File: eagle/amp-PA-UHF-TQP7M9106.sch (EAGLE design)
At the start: 27 parts, among them Q3 MOSFET-P-N-PAIR, U1 TQP7M9106, X1 SMA-142-0701-801/806, X2 SMA-142-0701-801/806

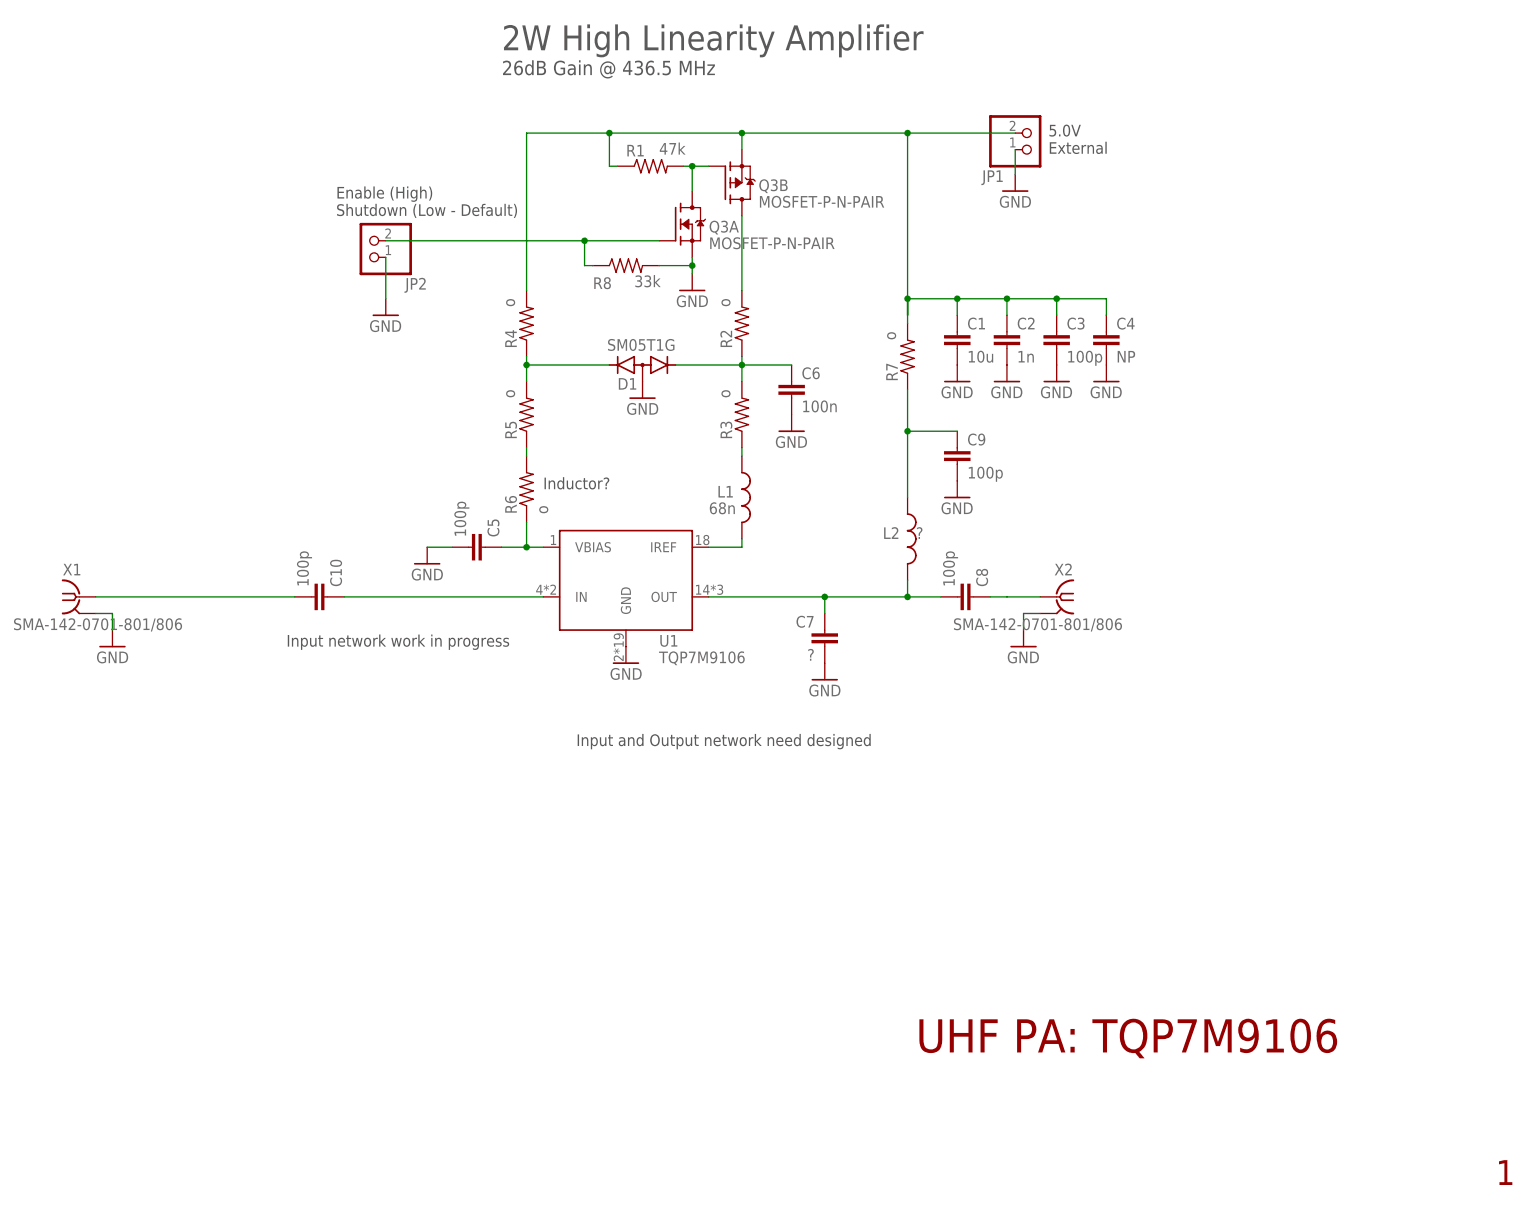
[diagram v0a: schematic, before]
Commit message: PA TQP7M9206, some updates, desgin will most likely use TQP7M9205
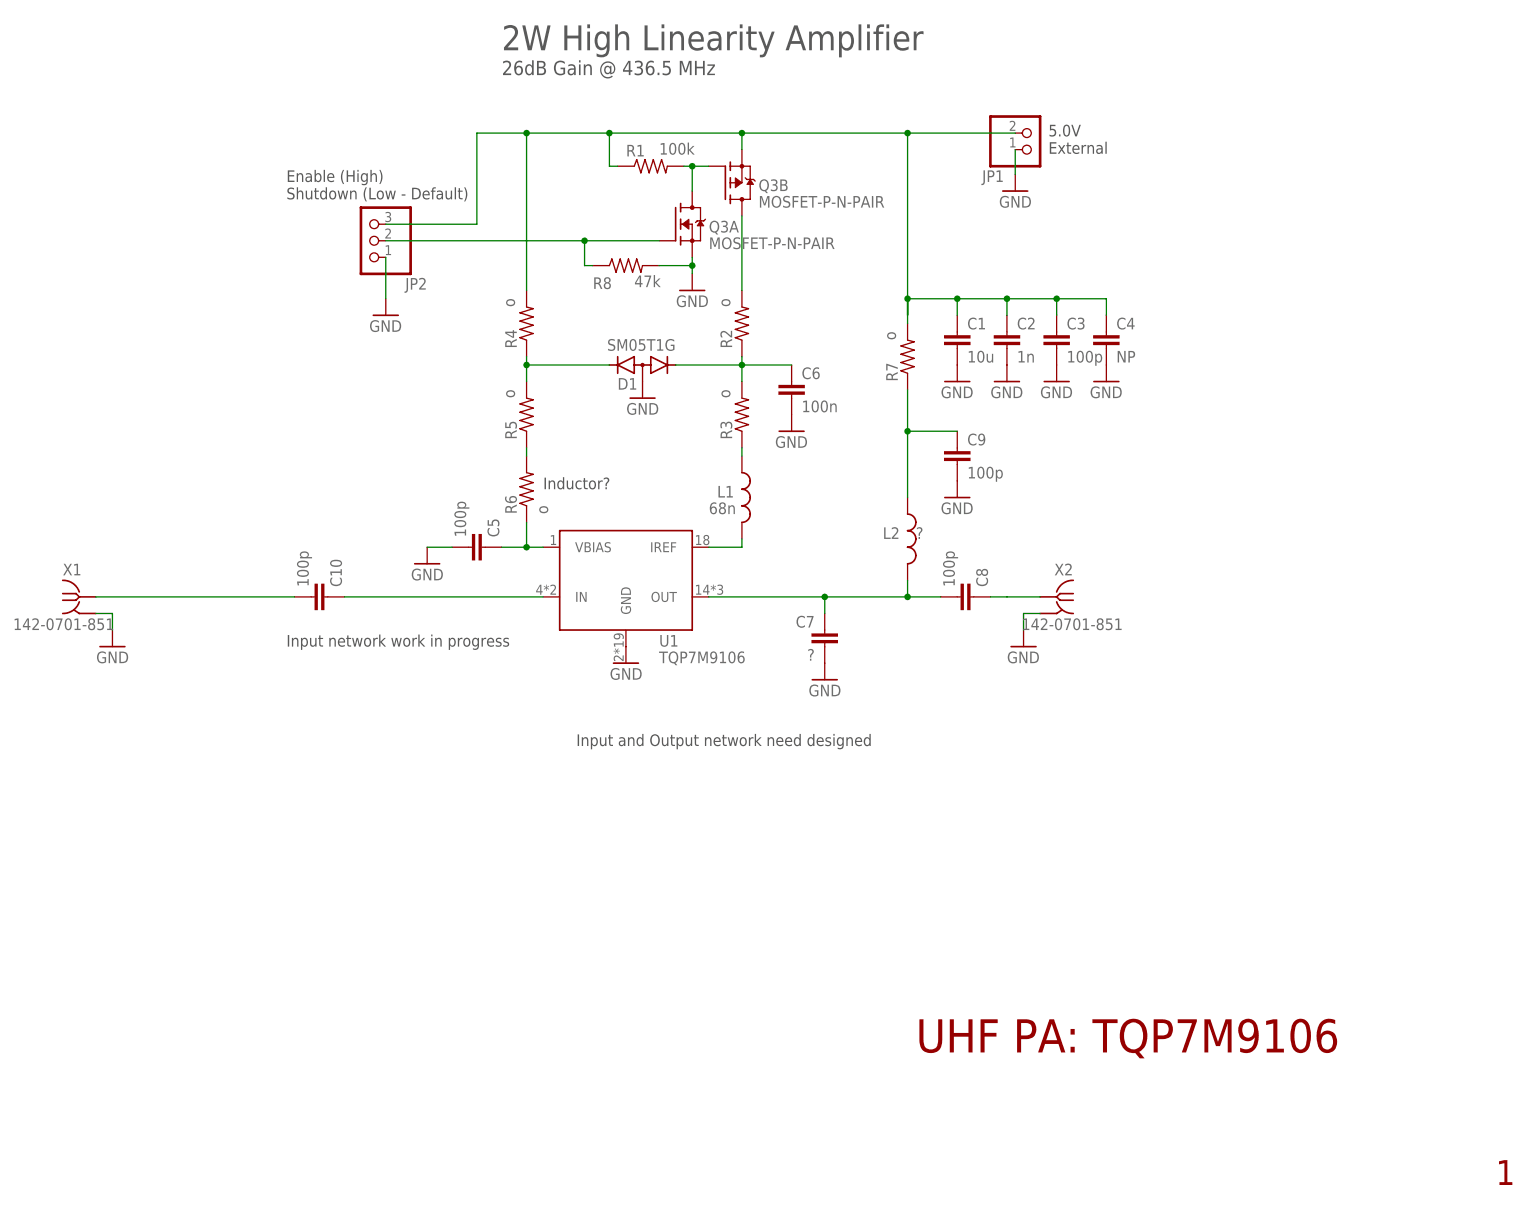
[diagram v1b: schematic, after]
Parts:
- JP2: device pinhead:PINHD-1X2 -> pinhead:PINHD-1X3
- R1: value 47k -> 100k
- R8: value 33k -> 47k
- X1, X2: value SMA-142-0701-801/806 -> 142-0701-851; device con-coax:SMA-142-0701-801/806 -> J-Cinch-142-0701-851-SMA-end-launch:142-0701-851
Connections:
- net GND: now also X1.GND, X2.GND; no longer X1.2, X2.2
- net N$6: now also X1.RF; no longer X1.1
- net N$67: now also X2.RF; no longer X2.1
- net N$72: now also JP2.3
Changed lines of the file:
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@@
 <part name="JP1" library="pinhead" library_urn="urn:adsk.eagle:library:325" deviceset="PINHD-1X2" device="" package3d_urn="urn:adsk.eagle:package:22435/2"/>
 <part name="GND70" library="supply1" library_urn="urn:adsk.eagle:library:371" deviceset="GND" device=""/>
-<part name="X1" library="con-coax" library_urn="urn:adsk.eagle:library:133" deviceset="SMA-" device="142-0701-801/806" package3d_urn="urn:adsk.eagle:package:6214/1"/>
+<part name="X1" library="J-Cinch-142-0701-851-SMA-end-launch" deviceset="142-0701-851" device=""/>
 <part name="GND71" library="supply1" library_urn="urn:adsk.eagle:library:371" deviceset="GND" device=""/>
 <part name="C8" library="oresat-rcl" deviceset="C-EU" device="0402-B-NOSILK" value="100p"/>
-<part name="X2" library="con-coax" library_urn="urn:adsk.eagle:library:133" deviceset="SMA-" device="142-0701-801/806" package3d_urn="urn:adsk.eagle:package:6214/1"/>
+<part name="X2" library="J-Cinch-142-0701-851-SMA-end-launch" deviceset="142-0701-851" device=""/>
 <part name="GND72" library="supply1" library_urn="urn:adsk.eagle:library:371" deviceset="GND" device=""/>
 <part name="L1" library="oresat-rcl" deviceset="L-US" device="0603-B-NOSILK" value="68n"/>
@@
 <part name="C3" library="oresat-rcl" deviceset="C-EU" device="0603-B-NOSILK" value="100p"/>
 <part name="GND103" library="supply1" library_urn="urn:adsk.eagle:library:371" deviceset="GND" device=""/>
-<part name="JP2" library="pinhead" library_urn="urn:adsk.eagle:library:325" deviceset="PINHD-1X2" device="" package3d_urn="urn:adsk.eagle:package:22435/2"/>
+<part name="JP2" library="pinhead" library_urn="urn:adsk.eagle:library:325" deviceset="PINHD-1X3" device="" package3d_urn="urn:adsk.eagle:package:22458/2"/>
 <part name="GND114" library="supply1" library_urn="urn:adsk.eagle:library:371" deviceset="GND" device=""/>
-<part name="R1" library="oresat-rcl" deviceset="R-US_" device="0402-B-NOSILK" value="47k"/>
+<part name="R1" library="oresat-rcl" deviceset="R-US_" device="0402-B-NOSILK" value="100k"/>
 <part name="R4" library="oresat-rcl" deviceset="R-US_" device="0805-B-NOSILK" value="o"/>
 <part name="R2" library="oresat-rcl" deviceset="R-US_" device="0805-B-NOSILK" value="o"/>
@@
 <part name="GND1" library="supply1" library_urn="urn:adsk.eagle:library:371" deviceset="GND" device=""/>
 <part name="C9" library="oresat-rcl" deviceset="C-EU" device="0603-B-NOSILK" value="100p"/>
-<part name="R8" library="oresat-rcl" deviceset="R-US_" device="0402-B-NOSILK" value="33k"/>
+<part name="R8" library="oresat-rcl" deviceset="R-US_" device="0402-B-NOSILK" value="47k"/>
 <part name="GND2" library="supply1" library_urn="urn:adsk.eagle:library:371" deviceset="GND" device=""/>
 <part name="Q3" library="Q-MOSFET-NP-Pair-SOT23-6" deviceset="MOSFET-P-N-PAIR" device=""/>
@@
 <text x="113.03" y="180.34" size="3.81" layer="97">2W High Linearity Amplifier</text>
 <text x="113.03" y="176.53" size="2.1844" layer="97">26dB Gain @ 436.5 MHz</text>
-<text x="87.63" y="154.94" size="1.778" layer="97">Enable (High)
+<text x="80.01" y="157.48" size="1.778" layer="97">Enable (High)
 Shutdown (Low - Default)</text>
 </plain>
@@
 <attribute name="VALUE" x="194.31" y="156.21" size="1.778" layer="96" rot="MR0"/>
 </instance>
-<instance part="X1" gate="G1" x="48.26" y="96.52" smashed="yes">
+<instance part="X1" gate="G$1" x="48.26" y="96.52" smashed="yes">
 <attribute name="VALUE" x="38.1" y="91.44" size="1.778" layer="96"/>
 <attribute name="NAME" x="45.72" y="99.822" size="1.778" layer="95"/>
@@
 <attribute name="VALUE" x="180.721" y="98.044" size="1.778" layer="96" rot="MR90"/>
 </instance>
-<instance part="X2" gate="G1" x="198.12" y="96.52" smashed="yes" rot="MR0">
+<instance part="X2" gate="G$1" x="198.12" y="96.52" smashed="yes" rot="MR0">
 <attribute name="VALUE" x="208.28" y="91.44" size="1.778" layer="96" rot="MR0"/>
 <attribute name="NAME" x="200.66" y="99.822" size="1.778" layer="95" rot="MR0"/>
@@
 <attribute name="VALUE" x="195.58" y="127" size="1.778" layer="96"/>
 </instance>
-<instance part="JP2" gate="G$1" x="92.71" y="151.13" smashed="yes" rot="R180">
+<instance part="JP2" gate="A" x="92.71" y="151.13" smashed="yes" rot="R180">
 <attribute name="NAME" x="101.6" y="145.415" size="1.778" layer="95" rot="R180"/>
 <attribute name="VALUE" x="99.06" y="156.21" size="1.778" layer="96" rot="R180"/>
@@
 </segment>
 <segment>
-<pinref part="X1" gate="G1" pin="2"/>
+<pinref part="X1" gate="G$1" pin="GND"/>
 <wire x1="53.34" y1="93.98" x2="50.8" y2="93.98" width="0.1524" layer="91"/>
 <pinref part="GND71" gate="1" pin="GND"/>
@@
 </segment>
 <segment>
-<pinref part="X2" gate="G1" pin="2"/>
+<pinref part="X2" gate="G$1" pin="GND"/>
 <wire x1="193.04" y1="93.98" x2="195.58" y2="93.98" width="0.1524" layer="91"/>
 <pinref part="GND72" gate="1" pin="GND"/>
@@
 <segment>
 <pinref part="GND114" gate="1" pin="GND"/>
-<pinref part="JP2" gate="G$1" pin="1"/>
+<pinref part="JP2" gate="A" pin="1"/>
 <wire x1="95.25" y1="142.24" x2="95.25" y2="148.59" width="0.1524" layer="91"/>
 </segment>
@@
 <net name="N$67" class="0">
 <segment>
-<pinref part="X2" gate="G1" pin="1"/>
+<pinref part="X2" gate="G$1" pin="RF"/>
 <wire x1="190.5" y1="96.52" x2="195.58" y2="96.52" width="0.1524" layer="91"/>
 <wire x1="190.5" y1="96.52" x2="187.96" y2="96.52" width="0.1524" layer="91"/>
@@
 <junction x="129.54" y="167.64"/>
 <pinref part="Q3" gate="B" pin="S"/>
+<pinref part="JP2" gate="A" pin="3"/>
+<wire x1="95.25" y1="153.67" x2="109.22" y2="153.67" width="0.1524" layer="91"/>
+<wire x1="109.22" y1="153.67" x2="109.22" y2="167.64" width="0.1524" layer="91"/>
+<wire x1="109.22" y1="167.64" x2="116.84" y2="167.64" width="0.1524" layer="91"/>
+<junction x="116.84" y="167.64"/>
 </segment>
 </net>
@@
 <wire x1="125.73" y1="151.13" x2="95.25" y2="151.13" width="0.1524" layer="91"/>
 <junction x="125.73" y="151.13"/>
-<pinref part="JP2" gate="G$1" pin="2"/>
+<pinref part="JP2" gate="A" pin="2"/>
 <pinref part="Q3" gate="A" pin="G"/>
 </segment>
@@
 <net name="N$6" class="0">
 <segment>
-<pinref part="X1" gate="G1" pin="1"/>
+<pinref part="X1" gate="G$1" pin="RF"/>
 <pinref part="C10" gate="CE" pin="2"/>
 <wire x1="50.8" y1="96.52" x2="81.28" y2="96.52" width="0.1524" layer="91"/>
